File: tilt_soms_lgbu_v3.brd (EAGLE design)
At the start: 36 x 118 mm, 30 parts

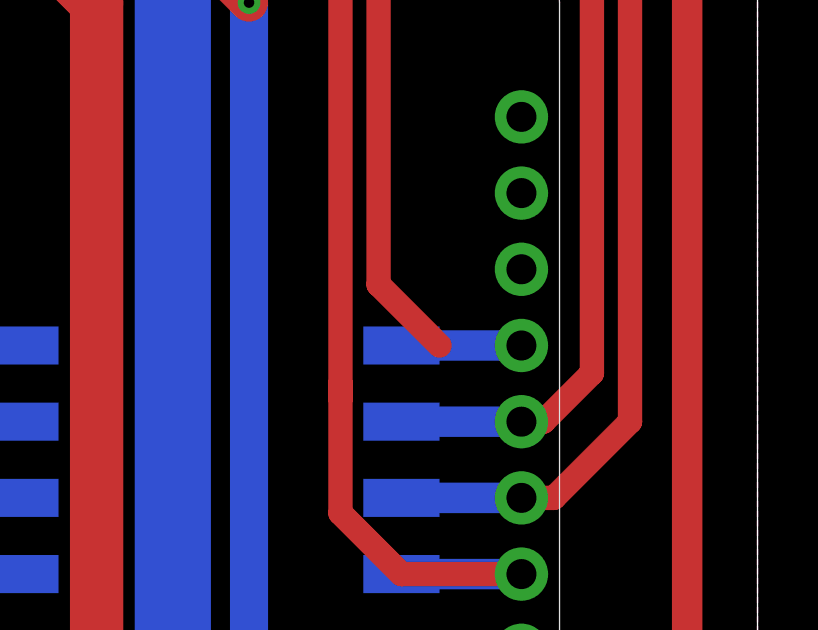
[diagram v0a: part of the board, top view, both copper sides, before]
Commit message: fixed unrouted trace
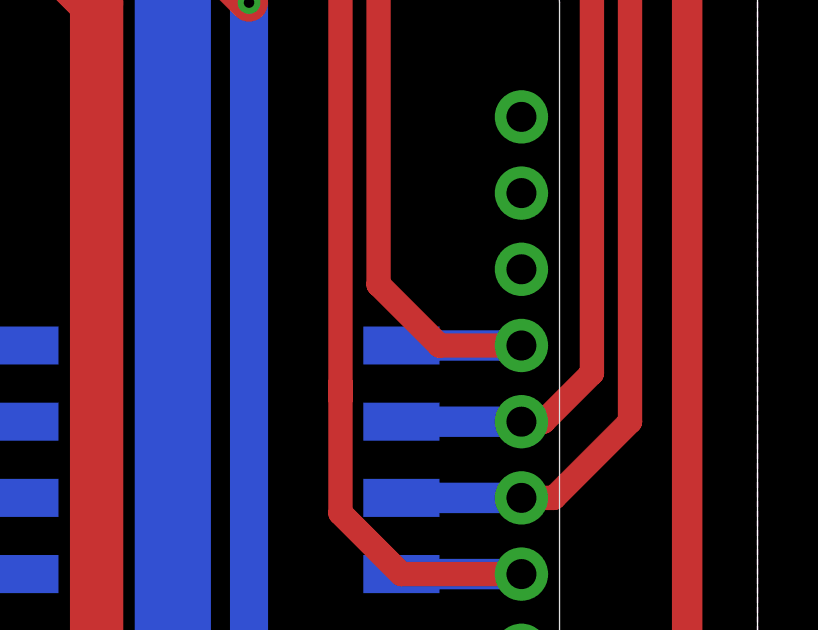
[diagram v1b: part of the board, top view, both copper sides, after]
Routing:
- net MISO: track 33.5 -> 36.2 mm
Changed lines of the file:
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@@
 <grid distance="50" unitdist="mil" unit="mil" style="lines" multiple="1" display="no" altdistance="5" altunitdist="mil" altunit="mil"/>
 <layers>
-<layer number="1" name="Top" color="4" fill="1" visible="yes" active="yes"/>
-<layer number="16" name="Bottom" color="1" fill="1" visible="yes" active="yes"/>
-<layer number="17" name="Pads" color="2" fill="1" visible="yes" active="yes"/>
-<layer number="18" name="Vias" color="2" fill="1" visible="yes" active="yes"/>
+<layer number="1" name="Top" color="4" fill="1" visible="no" active="yes"/>
+<layer number="16" name="Bottom" color="1" fill="1" visible="no" active="yes"/>
+<layer number="17" name="Pads" color="2" fill="1" visible="no" active="yes"/>
+<layer number="18" name="Vias" color="2" fill="1" visible="no" active="yes"/>
 <layer number="19" name="Unrouted" color="6" fill="1" visible="yes" active="yes"/>
-<layer number="20" name="Dimension" color="24" fill="1" visible="yes" active="yes"/>
-<layer number="21" name="tPlace" color="7" fill="1" visible="yes" active="yes"/>
+<layer number="20" name="Dimension" color="24" fill="1" visible="no" active="yes"/>
+<layer number="21" name="tPlace" color="7" fill="1" visible="no" active="yes"/>
 <layer number="22" name="bPlace" color="7" fill="1" visible="no" active="yes"/>
-<layer number="23" name="tOrigins" color="15" fill="1" visible="yes" active="yes"/>
+<layer number="23" name="tOrigins" color="15" fill="1" visible="no" active="yes"/>
 <layer number="24" name="bOrigins" color="15" fill="1" visible="no" active="yes"/>
-<layer number="25" name="tNames" color="7" fill="1" visible="yes" active="yes"/>
+<layer number="25" name="tNames" color="7" fill="1" visible="no" active="yes"/>
 <layer number="26" name="bNames" color="7" fill="1" visible="no" active="yes"/>
 <layer number="27" name="tValues" color="7" fill="1" visible="no" active="yes"/>
@@
 <layer number="35" name="tGlue" color="7" fill="4" visible="no" active="yes"/>
 <layer number="36" name="bGlue" color="7" fill="5" visible="no" active="yes"/>
-<layer number="37" name="tTest" color="7" fill="1" visible="yes" active="yes"/>
+<layer number="37" name="tTest" color="7" fill="1" visible="no" active="yes"/>
 <layer number="38" name="bTest" color="7" fill="1" visible="no" active="yes"/>
-<layer number="39" name="tKeepout" color="4" fill="11" visible="yes" active="yes"/>
+<layer number="39" name="tKeepout" color="4" fill="11" visible="no" active="yes"/>
 <layer number="40" name="bKeepout" color="1" fill="11" visible="no" active="yes"/>
-<layer number="41" name="tRestrict" color="4" fill="10" visible="yes" active="yes"/>
+<layer number="41" name="tRestrict" color="4" fill="10" visible="no" active="yes"/>
 <layer number="42" name="bRestrict" color="1" fill="10" visible="no" active="yes"/>
 <layer number="43" name="vRestrict" color="2" fill="10" visible="no" active="yes"/>
 <layer number="44" name="Drills" color="7" fill="1" visible="no" active="yes"/>
-<layer number="45" name="Holes" color="7" fill="1" visible="yes" active="yes"/>
+<layer number="45" name="Holes" color="7" fill="1" visible="no" active="yes"/>
 <layer number="46" name="Milling" color="3" fill="1" visible="no" active="yes"/>
 <layer number="47" name="Measures" color="7" fill="1" visible="no" active="yes"/>
@@
 <layer number="49" name="Reference" color="7" fill="1" visible="no" active="yes"/>
 <layer number="50" name="dxf" color="7" fill="1" visible="no" active="no"/>
-<layer number="51" name="tDocu" color="7" fill="1" visible="yes" active="yes"/>
+<layer number="51" name="tDocu" color="7" fill="1" visible="no" active="yes"/>
 <layer number="52" name="bDocu" color="7" fill="1" visible="no" active="yes"/>
 <layer number="53" name="tGND_GNDA" color="7" fill="9" visible="no" active="no"/>
@@
 <contactref element="INCLINOMETER" pad="6"/>
 <contactref element="PAD26" pad="1"/>
-<wire x1="25.4" y1="46.99" x2="23.368" y2="49.022" width="0.8128" layer="1"/>
+<wire x1="23.368" y1="49.022" x2="25.4" y2="46.99" width="0.8128" layer="1"/>
 <wire x1="23.368" y1="71.882" x2="23.368" y2="49.022" width="0.8128" layer="1"/>
 <wire x1="20.5" y1="74.025" x2="21.225" y2="74.025" width="0.4064" layer="1"/>
@@
 <contactref element="MS2" pad="13"/>
 <wire x1="28.1305" y1="46.99" x2="24.13" y2="46.99" width="1.016" layer="16"/>
-<wire x1="24.13" y1="46.99" x2="25.4" y2="46.99" width="0" layer="19" extent="1-16"/>
+<wire x1="25.4" y1="46.99" x2="28.1305" y2="46.99" width="0.8128" layer="1"/>
 </signal>
 <signal name="CSB_EN">

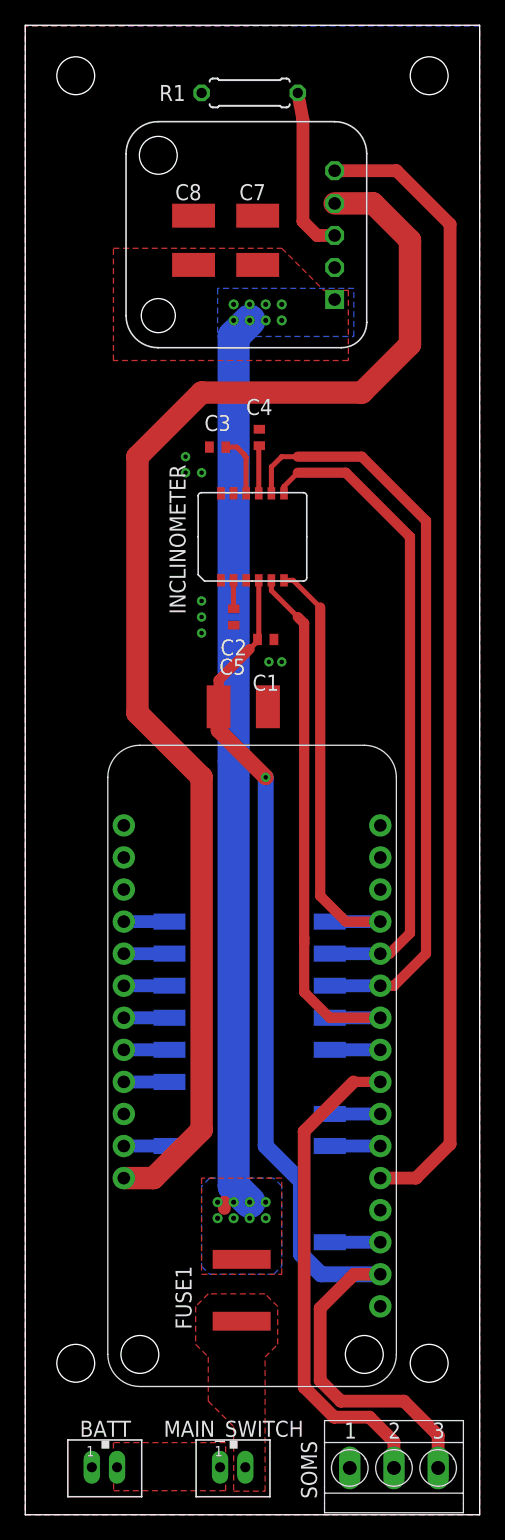
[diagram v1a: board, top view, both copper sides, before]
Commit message: edc modules - larger pad size for dcdc gateway - right package for capacitor and fuse tilt board - no more timer module, embedded design, right packages for caps and fuse
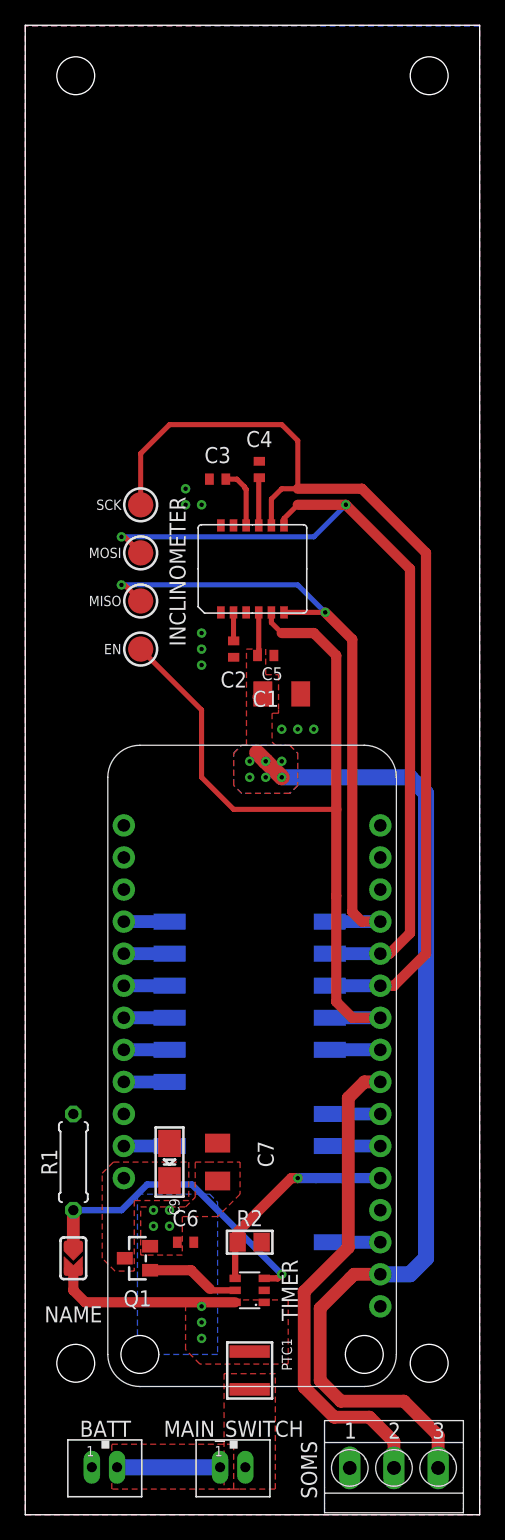
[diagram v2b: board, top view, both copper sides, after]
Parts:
- removed C8: (no value), rcl:C1812
- removed FUSE1: MF-SMDF200, fuse:MF-SMDF050
- removed U$3: TPL5110_BREAKOUT, edc_modules:TPL5110_BREAKOUT
- added C6: 0.1uF, rcl:C0402
- added C9: (no value), microbuilder:EIA3216-18/A-W
- added EN, MISO, MOSI, SCK: (no value), microbuilder:TESTPOINT_ROUND_2MM
- added PTC1: (no value), microbuilder:PTC1210
- added Q1: CMG3415, microbuilder:SOT23-WIDE
- added R2: (no value), microbuilder:0805
- added TIMER: TPL5110, edc_modules:SOT23-6
- added TRIG: (no value), microbuilder:SOLDERJUMPER_ARROW_NOPASTE
- C5, C7: device rcl:C1812 -> rcl:C1206K
- moved R1 85.8 mm to (3.81, 27.9), turned to 270 degrees
- moved C7 73.1 mm to (15.2, 27.9)
- moved C5 3.21 mm to (20.3, 65.0)
- moved C2 2.54 mm to (16.5, 68.6)
- moved C3 2.54 mm to (15.2, 82.0)
- moved C4 2.54 mm to (18.5, 82.8)
- moved INCLINOMETER 2.54 mm to (18.0, 74.9)
- moved C1 1.27 mm to (19.1, 68.1)
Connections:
- removed net VOLTAGE_SUPPLY: C7.1, C8.1, FUSE1.2, U$3.VDD
- new net N$6: Q1.1, TIMER.5
- new net VBAT: C6.1, C7.1, PTC1.P$1, Q1.2, TIMER.1, TIMER.6, TRIG.2
- net CSB_EN: now also EN.P$1
- net DELAY: now also TIMER.3, TRIG.1; no longer U$3.DELAY
- net DONE_PIN: now also R2.2, TIMER.4; no longer U$3.DONE
- net FEATHER_BAT: now also C9.+, Q1.3; no longer U$3.DRV
- net GND: now also C6.2, C9.-, R2.1, TIMER.2; no longer C8.2, U$3.GND
- net MISO: now also MISO.P$1
- net MOSI: now also MOSI.P$1
- net N$4: now also PTC1.P$2; no longer FUSE1.1
- net SCK: now also SCK.P$1
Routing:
- net FEATHER_BAT: track 103.9 -> 0.00 mm
- net DONE_PIN: track 90.4 -> 16.8 mm, vias 0 -> 1
- net VOLTAGE_SUPPLY: track 71.4 -> 0.00 mm, vias 16 -> 0
- net CSB_EN: track 45.1 -> 66.4 mm
- net SCK: track 59.7 -> 79.0 mm
- net MOSI: track 51.5 -> 69.8 mm, vias 0 -> 2
- net MISO: track 36.2 -> 53.5 mm, vias 0 -> 2
- net VBAT: track 0.00 -> 14.7 mm, vias 0 -> 7
- net DELAY: track 13.2 -> 24.6 mm, vias 0 -> 1
- net N$3: track 0.00 -> 8.16 mm
- net N$6: track 0.00 -> 7.40 mm
- net +3V3: track 89.7 -> 85.9 mm, vias 1 -> 6
- added copper zone on layer 1, net +3V3
- added copper zone on layer 16, net +3V3
- added copper zone on layer 1, net FEATHER_BAT
- added copper zone on layer 1, net VBAT
- added copper zone on layer 16, net VBAT
- removed copper zone on layer 1, net VOLTAGE_SUPPLY
- removed copper zone on layer 16, net VOLTAGE_SUPPLY

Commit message: ferrite bead, pull ups, standard battery header
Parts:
- removed MAIN_SWITCH: JST-PH_2-PIN_HEADER, SRG:JST_B2B-PH_HEADER
- added L1: BLM15HG601SN1, inductors:0402
- added MAINS: JST-PH_2-PIN_HEADER, SRG:JST_B2B-PH_HEADER
- added R3, R4: (no value), microbuilder:0805
- added TRIG_TEST: (no value), microbuilder:SOLDERJUMPER_ARROW_NOPASTE
- BATT: value JST-PH_2-PIN_HEADER -> (none); device SRG:JST_B2B-PH_HEADER -> SparkFun-Connectors:MOLEX-1X2_LOCK
- R1: device rcl:0207/7 -> rcl:0207/10
- TRIG: value (none) -> JST-PH_2-PIN_HEADER; device microbuilder:SOLDERJUMPER_ARROW_NOPASTE -> SRG:JST_B2B-PH_HEADER
- moved TRIG 21.6 mm to (19.3, 5.33), turned to 180 degrees
- moved PTC1 1.61 mm to (16.3, 11.9)
- moved BATT 1.27 mm to (6.35, 5.08)
- moved R1 1.27 mm to (3.81, 29.2)
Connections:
- new net N$7: C1.1, C5.1, INCLINOMETER.4, L1.1
- net +3V3: now also L1.2, R3.2, R4.2; no longer C1.1, C5.1, INCLINOMETER.4
- net DELAY: now also TRIG.P1, TRIG_TEST.1; no longer TRIG.1
- net GND: now also BATT.2; no longer BATT.P1
- net MISO: now also R3.1
- net MOSI: now also R4.1
- net N$3: now also BATT.1, MAINS.P1; no longer BATT.P2, MAIN_SWITCH.P1
- net N$4: now also MAINS.P2; no longer MAIN_SWITCH.P2
- net VBAT: now also TRIG.P2, TRIG_TEST.2; no longer TRIG.2
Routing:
- net DELAY: track 24.6 -> 38.3 mm
- net +3V3: track 85.9 -> 96.1 mm, vias 6 -> 7
- net VBAT: track 14.7 -> 23.7 mm
- net N$3: track 8.16 -> 0.00 mm
- net MOSI: track 69.8 -> 75.1 mm
- net N$7: track 0.00 -> 3.45 mm
- net MISO: track 53.5 -> 56.5 mm
- net SCK: track 79.0 -> 80.2 mm
- added copper zone on layer 1, net N$7
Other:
- board size 36 x 118 mm -> 36 x 90 mm
- board text added: "Tilt and Soil Moisture Board v3"

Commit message: tilt_soms_lgbu_v3.brd minor changes
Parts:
- moved MAINS 1.02 mm to (11.2, 5.33)
- moved BATT 0.76 mm to (5.59, 5.08)
- moved TRIG 0.76 mm to (18.5, 5.33)
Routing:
- net VBAT: track 23.7 -> 23.2 mm
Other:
- board text added: "G"
- board text added: "R"
- board text added: "W"
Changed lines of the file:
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@@
 <grid distance="10" unitdist="mil" unit="mil" style="lines" multiple="1" display="yes" altdistance="5" altunitdist="mil" altunit="mil"/>
 <layers>
-<layer number="1" name="Top" color="4" fill="1" visible="yes" active="yes"/>
-<layer number="16" name="Bottom" color="1" fill="1" visible="no" active="yes"/>
+<layer number="1" name="Top" color="4" fill="1" visible="no" active="yes"/>
+<layer number="16" name="Bottom" color="1" fill="1" visible="yes" active="yes"/>
 <layer number="17" name="Pads" color="2" fill="1" visible="yes" active="yes"/>
 <layer number="18" name="Vias" color="2" fill="1" visible="yes" active="yes"/>
@@
 <dimension x1="-1" y1="0" x2="-1" y2="90" x3="-4" y3="45" textsize="1.778" layer="51"/>
 <dimension x1="0" y1="-1" x2="36" y2="-1" x3="18" y3="-5" textsize="1.778" layer="51"/>
+<text x="25.654" y="7.874" size="1.27" layer="21" font="vector" ratio="10" align="bottom-center">G</text>
+<text x="29.21" y="7.874" size="1.27" layer="21" font="vector" ratio="10" align="bottom-center">R</text>
+<text x="32.766" y="7.874" size="1.27" layer="21" font="vector" ratio="10" align="bottom-center">W</text>
 </plain>
 <attributes>
@@
 <attribute name="VALUE" x="19.05" y="26.035" size="1.27" layer="27" rot="R90"/>
 </element>
-<element name="MAINS" library="SRG" package="JST_B2B-PH_HEADER" value="JST-PH_2-PIN_HEADER" x="12.192" y="5.334" smashed="yes" rot="R180">
-<attribute name="NAME" x="12.192" y="8.334" size="1.27" layer="25" font="vector" ratio="10" rot="R180" align="center"/>
+<element name="MAINS" library="SRG" package="JST_B2B-PH_HEADER" value="JST-PH_2-PIN_HEADER" x="11.176" y="5.334" smashed="yes" rot="R180">
+<attribute name="NAME" x="11.176" y="8.334" size="1.27" layer="25" font="vector" ratio="10" rot="R180" align="center"/>
 </element>
 <element name="PAD13" library="wirepad" library_urn="urn:adsk.eagle:library:412" package="SMD1,27-2,54" package3d_urn="urn:adsk.eagle:package:30839/1" value="WIREPADSMD1,27-254" x="24.13" y="21.59" smashed="yes" rot="MR270"/>
@@
 </element>
 <element name="SOMS" library="Rembrandt Electronics - Terminal Block 3-5mm v1-0" package="TERMINAL-BLOCK-3-PIN-3.5MM-LONG-PAD" value="TERMINAL-BLOCK-3.5MM-3-PIN-LONG-PAD" x="29.21" y="3.81" smashed="yes">
-<attribute name="NAME" x="24.13" y="8.636" size="1.27" layer="25" font="vector" ratio="10"/>
+<attribute name="NAME" x="23.368" y="2.794" size="1.27" layer="25" font="vector" ratio="10" rot="R90"/>
 <attribute name="VALUE" x="25.4075" y="7.9375" size="1.27" layer="27"/>
 </element>
@@
 <element name="R3" library="microbuilder" package="0805" value="" x="26.67" y="73.66"/>
 <element name="R4" library="microbuilder" package="0805" value="" x="26.67" y="76.2"/>
-<element name="TRIG" library="SRG" package="JST_B2B-PH_HEADER" value="JST-PH_2-PIN_HEADER" x="19.304" y="5.334" smashed="yes" rot="R180">
-<attribute name="NAME" x="19.304" y="7.62" size="1.27" layer="25" font="vector" ratio="10" align="bottom-center"/>
-</element>
-<element name="BATT" library="SparkFun-Connectors" package="MOLEX-1X2_LOCK" value="" x="6.35" y="5.08" smashed="yes" rot="R180">
-<attribute name="NAME" x="5.08" y="7.874" size="1.27" layer="25" font="vector" ratio="10" align="bottom-center"/>
-<attribute name="SF_ID" value="PRT-09918" x="6.35" y="5.08" size="1.778" layer="27" rot="R180" display="off"/>
-<attribute name="VALUE" x="7.62" y="7.874" size="0.6096" layer="27" font="vector" ratio="20" rot="R180" align="top-left"/>
+<element name="TRIG" library="SRG" package="JST_B2B-PH_HEADER" value="JST-PH_2-PIN_HEADER" x="18.542" y="5.334" smashed="yes" rot="R180">
+<attribute name="NAME" x="18.542" y="7.62" size="1.27" layer="25" font="vector" ratio="10" align="bottom-center"/>
+</element>
+<element name="BATT" library="SparkFun-Connectors" package="MOLEX-1X2_LOCK" value="" x="5.588" y="5.08" smashed="yes" rot="R180">
+<attribute name="NAME" x="4.318" y="7.874" size="1.27" layer="25" font="vector" ratio="10" align="bottom-center"/>
+<attribute name="SF_ID" value="PRT-09918" x="5.588" y="5.08" size="1.778" layer="27" rot="R180" display="off"/>
+<attribute name="VALUE" x="6.858" y="7.874" size="0.6096" layer="27" font="vector" ratio="20" rot="R180" align="top-left"/>
 </element>
 </elements>
@@
 <via x="20.32" y="19.05" extent="1-16" drill="0.35"/>
 <contactref element="TRIG" pad="P1"/>
-<wire x1="18.229" y1="5.2865" x2="18.229" y2="9.711" width="0.8128" layer="16"/>
+<wire x1="17.467" y1="5.2865" x2="17.467" y2="10.473" width="0.8128" layer="16"/>
 <wire x1="13.53979375" y1="12.9314" x2="12.9314" y2="13.53979375" width="0.8128" layer="16"/>
 <wire x1="12.9314" y1="15.0086" x2="3.81" y2="24.13" width="0.8128" layer="16"/>
-<wire x1="18.229" y1="9.711" x2="15.0086" y2="12.9314" width="0.8128" layer="16"/>
+<wire x1="17.467" y1="10.473" x2="15.0086" y2="12.9314" width="0.8128" layer="16"/>
 <wire x1="15.0086" y1="12.9314" x2="13.53979375" y2="12.9314" width="0.8128" layer="16"/>
 <wire x1="12.9314" y1="13.53979375" x2="12.9314" y2="15.0086" width="0.8128" layer="16"/>
@@
 <contactref element="MAINS" pad="P2"/>
 <contactref element="PTC1" pad="P$2"/>
-<polygon width="0.254" layer="1">
-<vertex x="13.97" y="3.302"/>
-<vertex x="13.97" y="9.144"/>
-<vertex x="18.288" y="9.144"/>
+<polygon width="0.1524" layer="1">
+<vertex x="11.176" y="3.302"/>
+<vertex x="12.954" y="3.302"/>
+<vertex x="12.954" y="8.382"/>
+<vertex x="13.97" y="9.398"/>
+<vertex x="18.288" y="9.398"/>
 <vertex x="18.288" y="11.43"/>
-<vertex x="14.224" y="11.43"/>
-<vertex x="12.446" y="11.43"/>
-<vertex x="12.446" y="3.302"/>
+<vertex x="12.954" y="11.43"/>
+<vertex x="11.176" y="9.652"/>
 </polygon>
 </signal>
@@
 <contactref element="MAINS" pad="P1"/>
 <polygon width="0.254" layer="1" rank="2">
-<vertex x="5.334" y="6.858"/>
-<vertex x="11.938" y="6.858"/>
-<vertex x="11.938" y="3.302"/>
-<vertex x="5.334" y="3.302"/>
+<vertex x="4.826" y="7.366"/>
+<vertex x="10.668" y="7.366"/>
+<vertex x="10.668" y="3.302"/>
+<vertex x="4.826" y="3.302"/>
 </polygon>
 <contactref element="BATT" pad="1"/>
@@
 <contactref element="C7" pad="1"/>
 <polygon width="0.1524" layer="1">
-<vertex x="20.828" y="12.446"/>
-<vertex x="13.335" y="12.446"/>
+<vertex x="20.828" y="12.192"/>
+<vertex x="13.589" y="12.192"/>
 <vertex x="12.7" y="13.081"/>
 <vertex x="12.7" y="17.018"/>
@@
 <contactref element="PTC1" pad="P$1"/>
 <contactref element="TRIG" pad="P2"/>
-<wire x1="20.229" y1="5.2865" x2="20.229" y2="12.791" width="0.8128" layer="1"/>
-<wire x1="20.229" y1="12.791" x2="20.066" y2="12.954" width="0.8128" layer="1"/>
-<wire x1="20.066" y1="12.954" x2="16.74" y2="12.954" width="0.4064" layer="1"/>
+<wire x1="19.467" y1="5.2865" x2="19.467" y2="12.863" width="0.8128" layer="1"/>
+<wire x1="19.467" y1="12.863" x2="19.558" y2="12.954" width="0.8128" layer="1"/>
+<wire x1="19.558" y1="12.954" x2="19.467" y2="12.954" width="0.8128" layer="1"/>
+<wire x1="19.467" y1="12.954" x2="16.74" y2="12.954" width="0.4064" layer="1"/>
 <wire x1="16.74" y1="12.954" x2="16.256" y2="13.438" width="0.4064" layer="1"/>
 <wire x1="4.76" y1="16.83" x2="13.396" y2="16.83" width="0.8128" layer="1"/>

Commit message: lengthen scl3300 pads, isolated pads for axel, all supply goes through a ferrite bead
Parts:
- removed EN, MISO, MOSI, SCK: (no value), microbuilder:TESTPOINT_ROUND_2MM
- added DVIO_VCC: (no value), microbuilder:SOLDERJUMPER_ARROW_NOPASTE
- added SJ1: (no value), jumper:SJ
- moved C2 1.78 mm to (14.7, 68.6), turned to 180 degrees
- moved R3 1.27 mm to (25.4, 73.7)
- moved R4 1.27 mm to (25.4, 76.2)
- moved C4 0.92 mm to (19.3, 82.3), turned to 0 degrees
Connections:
- new net DGND: C1.2, C2.2, C3.2, C4.2, C5.2, INCLINOMETER.1, INCLINOMETER.11, INCLINOMETER.12, INCLINOMETER.3, SJ1.1
- net +3V3: no longer R3.2, R4.2
- net CSB_EN: no longer EN.P$1
- net GND: now also SJ1.2; no longer C1.2, C2.2, C3.2, C4.2, C5.2, INCLINOMETER.1, INCLINOMETER.11, INCLINOMETER.12, INCLINOMETER.3
- net MISO: no longer MISO.P$1
- net MOSI: no longer MOSI.P$1
- net N$5: now also DVIO_VCC.1
- net N$7: now also DVIO_VCC.2, R3.2, R4.2
- net SCK: no longer SCK.P$1
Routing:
- net N$7: track 3.45 -> 48.0 mm, vias 0 -> 2
- net CSB_EN: track 66.4 -> 42.5 mm
- net SCK: track 80.2 -> 58.1 mm
- net MOSI: track 75.1 -> 53.9 mm, vias 2 -> 0
- net MISO: track 56.5 -> 36.9 mm, vias 2 -> 0
- net +3V3: track 96.1 -> 78.3 mm, vias 7 -> 6
- net N$5: track 3.80 -> 10.8 mm
- net N$1: track 2.26 -> 3.12 mm
- added copper zone on layer 1, net DGND
- added copper zone on layer 16, net DGND
